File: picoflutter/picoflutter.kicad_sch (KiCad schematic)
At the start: 67 parts, among them IC1 AP7361EA-33E-13, IC3 W25Q64JVZPIQ, J2 SM04B-SRSS-TB, J4 S2B-PH-SM4-TB(LF)(SN), J5 USB4105-GF-A, Q1 DMG3415, SW2 MK-12C02-G020, U1 MCP73831T-2ACI/OT, U3 RP2040, Y1 445I23D12M00000

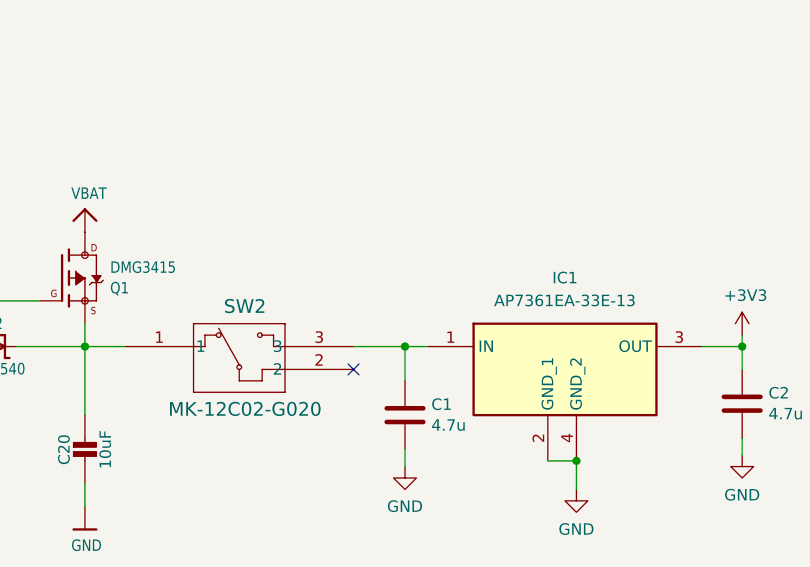
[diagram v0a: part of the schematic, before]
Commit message: fixed leds power supply
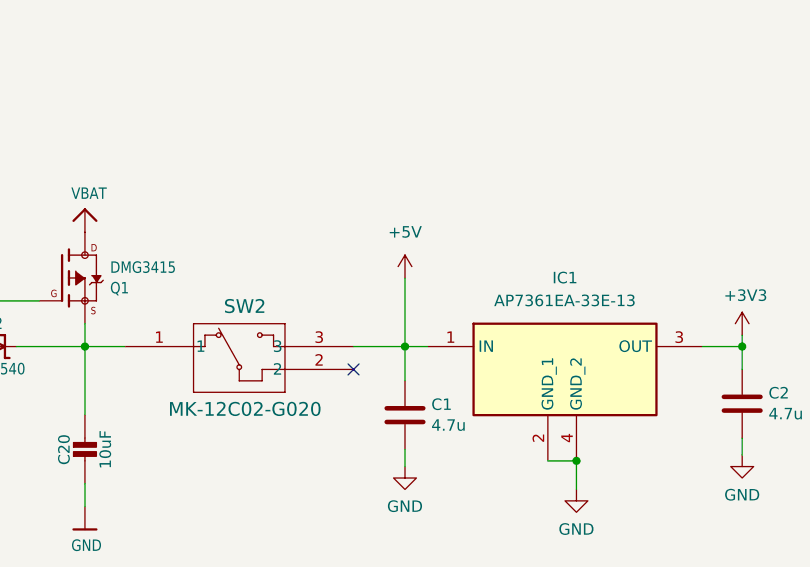
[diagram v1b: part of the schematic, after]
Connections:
- net +5V: now also C1.1, IC1.1 (IN), SW2.3
